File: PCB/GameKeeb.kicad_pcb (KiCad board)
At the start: 2 copper layers, 40.3 x 65.2 mm, 56 parts, among them J1 USB C Connector, J2 JTAG_TC2030, J3 USB_C_Receptacle_USB2.0, J4 USB_A, J5 GCC Cable, J6 Conn_01x10_Pin, SW1 Boot, U1 XC6206, U2 USBLC6-2SC6, U3 RP2040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

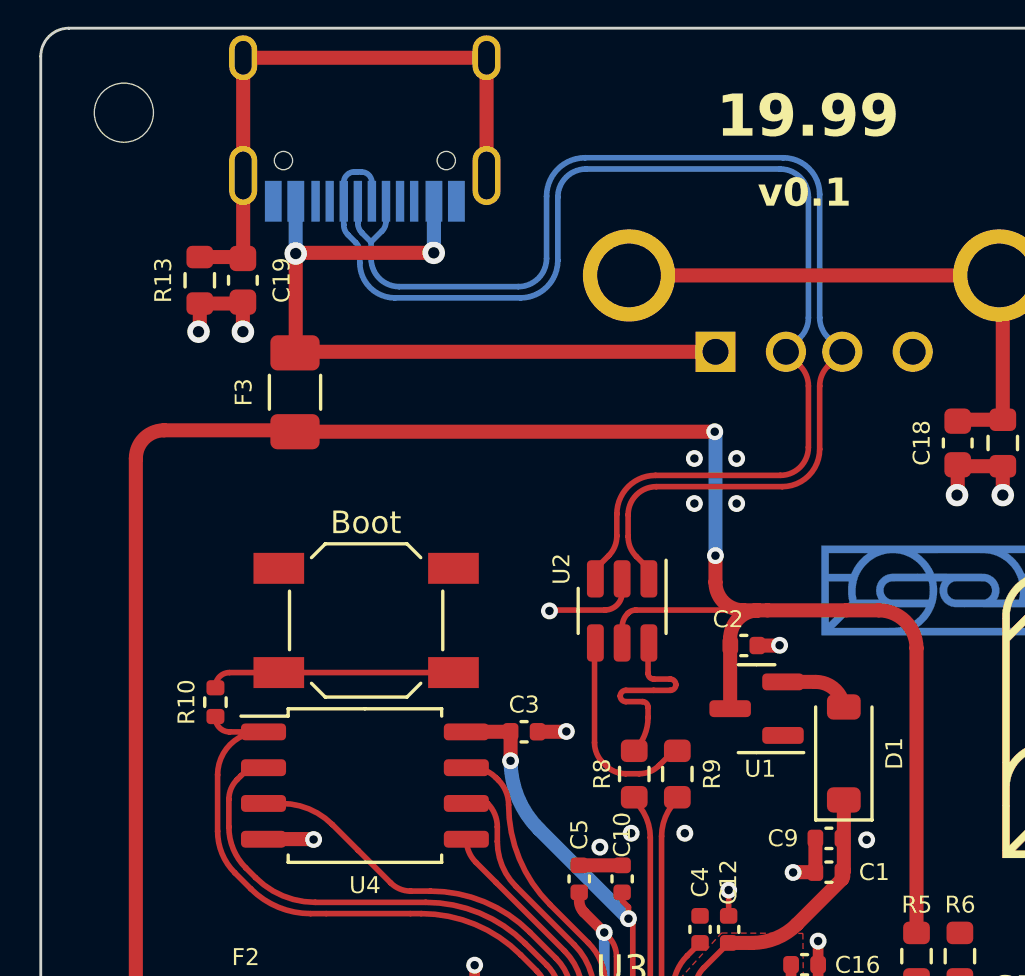
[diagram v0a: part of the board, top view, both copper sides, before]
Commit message: Moved boot button a little to the top
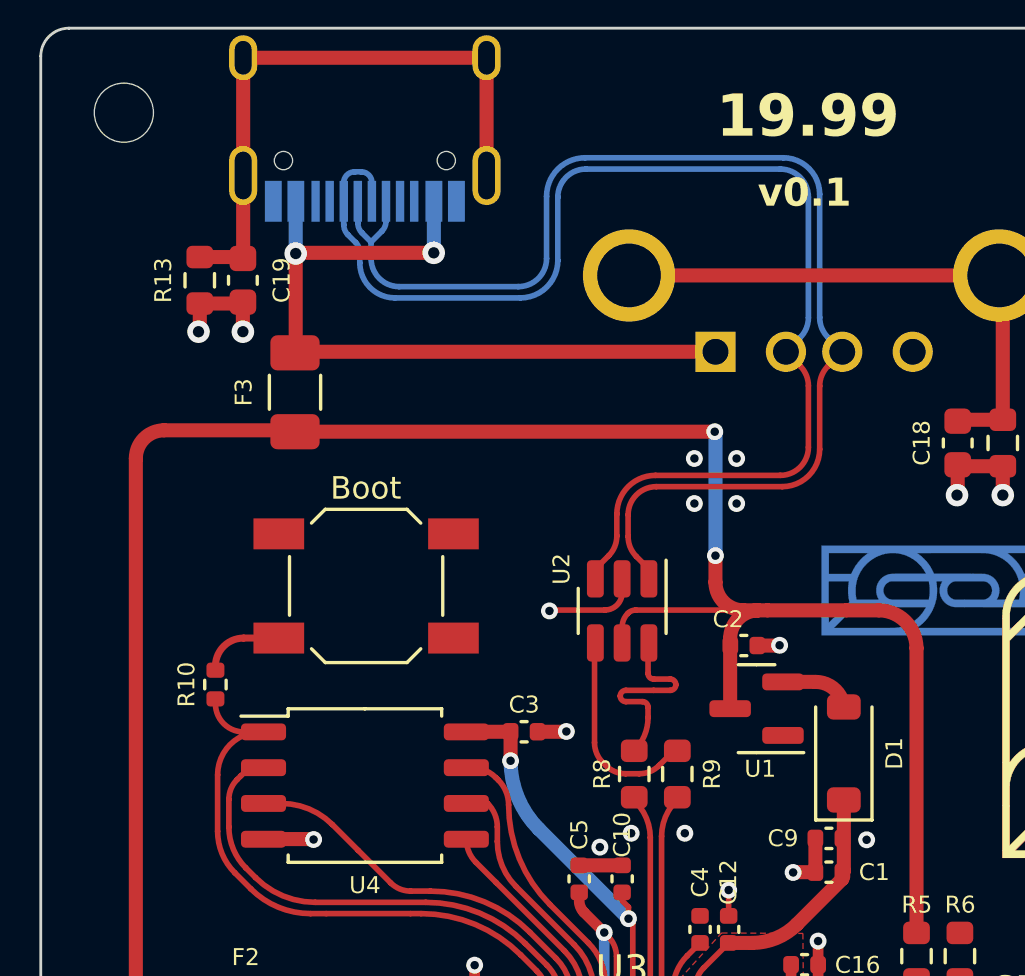
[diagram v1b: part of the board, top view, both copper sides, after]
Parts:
- moved SW1 1.23 mm to (37.5, 36.7)
- moved R10 0.62 mm to (32.1, 40.2)
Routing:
- net /~{USB_BOOT}: track 9.03 -> 2.92 mm
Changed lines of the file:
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@@
   )
   (footprint "Button_Switch_SMD:SW_SPST_SKQG_WithStem" (layer "F.Cu")
-    (at 37.45 37.9)
+    (at 37.45 36.675)
     (descr "ALPS 5.2mm Square Low-profile Type (Surface Mount) SKQG Series, With stem, http://www.alps.com/prod/info/E/HTML/Tact/SurfaceMount/SKQG/SKQGAFE010.html")
     (tags "SPST Button Switch")
@@
       (polygon
         (pts
-          (xy 33.45 36.6)
-          (xy 36.45 36.6)
-          (xy 36.45 39.2)
-          (xy 33.45 39.2)
+          (xy 33.45 35.375)
+          (xy 36.45 35.375)
+          (xy 36.45 37.975)
+          (xy 33.45 37.975)
         )
       )
@@
       (polygon
         (pts
-          (xy 38.45 36.6)
-          (xy 41.45 36.6)
-          (xy 41.45 39.2)
-          (xy 38.45 39.2)
+          (xy 38.45 35.375)
+          (xy 41.45 35.375)
+          (xy 41.45 37.975)
+          (xy 38.45 37.975)
         )
       )
@@
   )
   (footprint "Resistor_SMD:R_0402_1005Metric" (layer "F.Cu")
-    (at 32.1 40.8 -90)
+    (at 32.1 40.175 -90)
     (descr "Resistor SMD 0402 (1005 Metric), square (rectangular) end terminal, IPC_7351 nominal, (Body size source: IPC-SM-782 page 72, https://www.pcb-3d.com/wordpress/wp-content/uploads/ipc-sm-782a_amendment_1_and_2.pdf), generated with kicad-footprint-generator")
     (tags "resistor")
@@
   (via (at 47.525089 67.790107) (size 0.6) (drill 0.3) (layers "F.Cu" "B.Cu") (net 1))
   (via (at 44.557339 41.841089) (size 0.6) (drill 0.3) (layers "F.Cu" "B.Cu") (net 1))
-  (via (at 49.103 32.1505) (size 0.6) (drill 0.3) (layers "F.Cu" "B.Cu") (free) (net 1))
+  (via (at 49.1025 32.1505) (size 0.6) (drill 0.3) (layers "F.Cu" "B.Cu") (free) (net 1))
   (via (at 48.763339 45.453982) (size 0.6) (drill 0.3) (layers "F.Cu" "B.Cu") (free) (net 1))
   (via (at 50.319089 47.470107) (size 0.6) (drill 0.3) (layers "F.Cu" "B.Cu") (net 1))
   (via (at 43.957339 37.561089) (size 0.6) (drill 0.3) (layers "F.Cu" "B.Cu") (net 1))
   (via (at 41.302089 50.137107) (size 0.6) (drill 0.3) (layers "F.Cu" "B.Cu") (net 1))
-  (via (at 49.103 33.7495) (size 0.6) (drill 0.3) (layers "F.Cu" "B.Cu") (free) (net 1))
+  (via (at 49.1025 33.7495) (size 0.6) (drill 0.3) (layers "F.Cu" "B.Cu") (free) (net 1))
   (via (at 55.217339 45.686089) (size 0.6) (drill 0.3) (layers "F.Cu" "B.Cu") (free) (net 1))
   (via (at 46.858339 45.453982) (size 0.6) (drill 0.3) (layers "F.Cu" "B.Cu") (free) (net 1))
@@
   (via (at 39.270089 58.265107) (size 0.6) (drill 0.3) (layers "F.Cu" "B.Cu") (net 1))
   (via (at 40.822339 65.123107) (size 0.6) (drill 0.3) (layers "F.Cu" "B.Cu") (net 1))
-  (via (at 50.602 32.1505) (size 0.6) (drill 0.3) (layers "F.Cu" "B.Cu") (free) (net 1))
-  (via (at 50.602 33.7495) (size 0.6) (drill 0.3) (layers "F.Cu" "B.Cu") (free) (net 1))
+  (via (at 50.6015 32.1505) (size 0.6) (drill 0.3) (layers "F.Cu" "B.Cu") (free) (net 1))
+  (via (at 50.6015 33.7495) (size 0.6) (drill 0.3) (layers "F.Cu" "B.Cu") (free) (net 1))
   (arc (start 45.920708 37.531089) (mid 46.356732 37.350482) (end 46.537339 36.914458) (width 0.2) (layer "F.Cu") (net 1))
   (arc (start 45.537339 59.264618) (mid 45.457267 59.667166) (end 45.229242 60.00843) (width 0.2) (layer "F.Cu") (net 1))
@@
   (segment (start 46.915489 48.638507) (end 46.915489 50.753489) (width 0.2) (layer "F.Cu") (net 2))
   (segment (start 50.319089 49.347107) (end 51.14783 49.347107) (width 0.5) (layer "F.Cu") (net 2))
-  (segment (start 54.573947 44.271089) (end 54.407339 44.271089) (width 0.5) (layer "F.Cu") (net 2))
   (via (at 46.890089 61.313107) (size 0.6) (drill 0.3) (layers "F.Cu" "B.Cu") (net 2))
   (via (at 46.763089 48.486107) (size 0.6) (drill 0.3) (layers "F.Cu" "B.Cu") (net 2))
@@
   (segment (start 37.655 22.356918) (end 37.655 23.02) (width 0.2) (layer "B.Cu") (net 12))
   (segment (start 52.15 21.875) (end 45.254657 21.875) (width 0.2) (layer "B.Cu") (net 12))
-  (segment (start 37.155 21.975) (end 37.273082 21.975) (width 0.2) (layer "B.Cu") (net 12))
   (segment (start 42.927525 26.45) (end 38.47072 26.45) (width 0.2) (layer "B.Cu") (net 12))
-  (segment (start 37.155 21.975) (end 37.03928 21.975) (width 0.2) (layer "B.Cu") (net 12))
+  (segment (start 37.273082 21.975) (end 37.03928 21.975) (width 0.2) (layer "B.Cu") (net 12))
   (segment (start 36.655 23.02) (end 36.655 22.35928) (width 0.2) (layer "B.Cu") (net 12))
   (segment (start 52.3525 28.3625) (end 52.857107 27.857893) (width 0.2) (layer "B.Cu") (net 12))
-  (segment (start 37.155 21.975) (end 37.155 21.975) (width 0.2) (layer "B.Cu") (net 12))
   (arc (start 53.15 27.150786) (mid 53.07388 27.533469) (end 52.857107 27.857893) (width 0.2) (layer "B.Cu") (net 12))
   (arc (start 45.254657 21.875) (mid 44.54755 22.167893) (end 44.254657 22.875) (width 0.2) (layer "B.Cu") (net 12))
@@
   (segment (start 47.937339 51.668589) (end 47.937339 45.564566) (width 0.2) (layer "F.Cu") (net 29))
   (arc (start 47.937339 45.564566) (mid 48.074356 44.875736) (end 48.464547 44.291774) (width 0.2) (layer "F.Cu") (net 29))
-  (segment (start 34.35 39.75) (end 40.55 39.75) (width 0.2) (layer "F.Cu") (net 30))
-  (segment (start 34.625 39.75) (end 32.6 39.75) (width 0.2) (layer "F.Cu") (net 30))
-  (segment (start 32.1 40.25) (end 32.1 40.29) (width 0.2) (layer "F.Cu") (net 30))
-  (arc (start 32.6 39.75) (mid 32.246447 39.896447) (end 32.1 40.25) (width 0.2) (layer "F.Cu") (net 30))
+  (segment (start 34.35 38.525) (end 33.1 38.525) (width 0.25) (layer "F.Cu") (net 30))
+  (segment (start 32.1 39.525) (end 32.1 39.665) (width 0.25) (layer "F.Cu") (net 30))
+  (arc (start 33.1 38.525) (mid 32.392893 38.817893) (end 32.1 39.525) (width 0.25) (layer "F.Cu") (net 30))
   (segment (start 43.937339 51.638358) (end 43.937334 51.389098) (width 0.2) (layer "F.Cu") (net 31))
   (segment (start 39.401073 48.306185) (end 39.022243 48.306185) (width 0.2) (layer "F.Cu") (net 31))
   (segment (start 32.177339 43.381754) (end 32.177339 45.381387) (width 0.2) (layer "F.Cu") (net 31))
+  (segment (start 32.1 40.856089) (end 32.1 40.685) (width 0.2) (layer "F.Cu") (net 31))
   (segment (start 36.032435 48.306185) (end 39.022243 48.306185) (width 0.2) (layer "F.Cu") (net 31))
   (segment (start 33.807339 41.856089) (end 33.703004 41.856089) (width 0.2) (layer "F.Cu") (net 31))
   (segment (start 32.789262 46.858698) (end 33.35855 47.427986) (width 0.2) (layer "F.Cu") (net 31))
-  (segment (start 33.807339 41.856089) (end 32.6 41.856089) (width 0.2) (layer "F.Cu") (net 31))
   (segment (start 43.937339 51.668589) (end 43.937339 51.638358) (width 0.2) (layer "F.Cu") (net 31))
   (segment (start 35.47987 48.306665) (end 36.031955 48.306665) (width 0.2) (layer "F.Cu") (net 31))
-  (segment (start 32.1 41.356089) (end 32.1 41.31) (width 0.2) (layer "F.Cu") (net 31))
   (segment (start 43.500523 50.334571) (end 42.936603 49.770651) (width 0.2) (layer "F.Cu") (net 31))
+  (segment (start 33.807339 41.856089) (end 33.1 41.856089) (width 0.2) (layer "F.Cu") (net 31))
   (arc (start 33.35855 47.427986) (mid 34.33182 48.078304) (end 35.47987 48.306665) (width 0.2) (layer "F.Cu") (net 31))
   (arc (start 43.937334 51.389098) (mid 43.823805 50.818392) (end 43.500523 50.334571) (width 0.2) (layer "F.Cu") (net 31))
   (arc (start 39.401073 48.306185) (mid 41.314488 48.686788) (end 42.936603 49.770651) (width 0.2) (layer "F.Cu") (net 31))
-  (arc (start 32.1 41.356089) (mid 32.246447 41.709642) (end 32.6 41.856089) (width 0.2) (layer "F.Cu") (net 31))
   (arc (start 32.177339 43.381754) (mid 32.624196 42.302946) (end 33.703004 41.856089) (width 0.2) (layer "F.Cu") (net 31))
+  (arc (start 33.1 41.856089) (mid 32.392893 41.563196) (end 32.1 40.856089) (width 0.2) (layer "F.Cu") (net 31))
   (arc (start 32.177339 45.381387) (mid 32.336372 46.180902) (end 32.789262 46.858698) (width 0.2) (layer "F.Cu") (net 31))
   (segment (start 46.337339 60.512125) (end 46.337339 58.543589) (width 0.2) (layer "F.Cu") (net 32))
